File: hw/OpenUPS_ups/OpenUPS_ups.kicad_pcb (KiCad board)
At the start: 4 copper layers, 96 x 64 mm, 332 parts, among them J1001 USB4105-GF-A, J101 Barrel Jack, J102 XT30PW-M, J103 B6B-PH-K_1x06, J105 S6B-PH-K_1x06, J106 Screw Terminal, J107 Screw Terminal, J108 Screw Terminal, J109 JST XH, J110 JST XH, J501 Conn_01x03, J701 0022053031, J702 0022053031, J901 Qwiic, J902 Qwiic, Q1001 2N7002, Q1101 AON7534, Q1102 AON7534, Q1103 BSS84, Q1104 BSS84, Q1105 2N7002, Q1106 2N7002, Q1107 BSS84, Q301 AON7534, Q302 AON7534, Q303 AON7534, Q304 AON7534, Q401 2N7002, Q402 AON7534, Q403 AON7534, Q404 AON7534, Q405 AON7534, Q406 AON7423, Q601 AON7534, Q602 AON7534, Q603 AON7534, Q604 AON7534, Q701 2N7002, Q702 2N7002, U1001 MCP6547, U1002 AP22814BW5, U1003 NUP2301MW6T1G, U103 LM75BTP,147, U104 AVR64DB48x-x6LX, U1101 BQ76920PW, U1102 π220N31, U201 TPS51397A, U202 INA180A3, U301 NCP81599, U401 NCP431, U402 BD99950, U403 MCP6001R, U404 DZDH0401DW, U405 INA180A1, U601 NCP81599, U701 NUP2301MW6T1G, U702 NUP2301MW6T1G, U801 AP7383-33W5, U901 π220N31

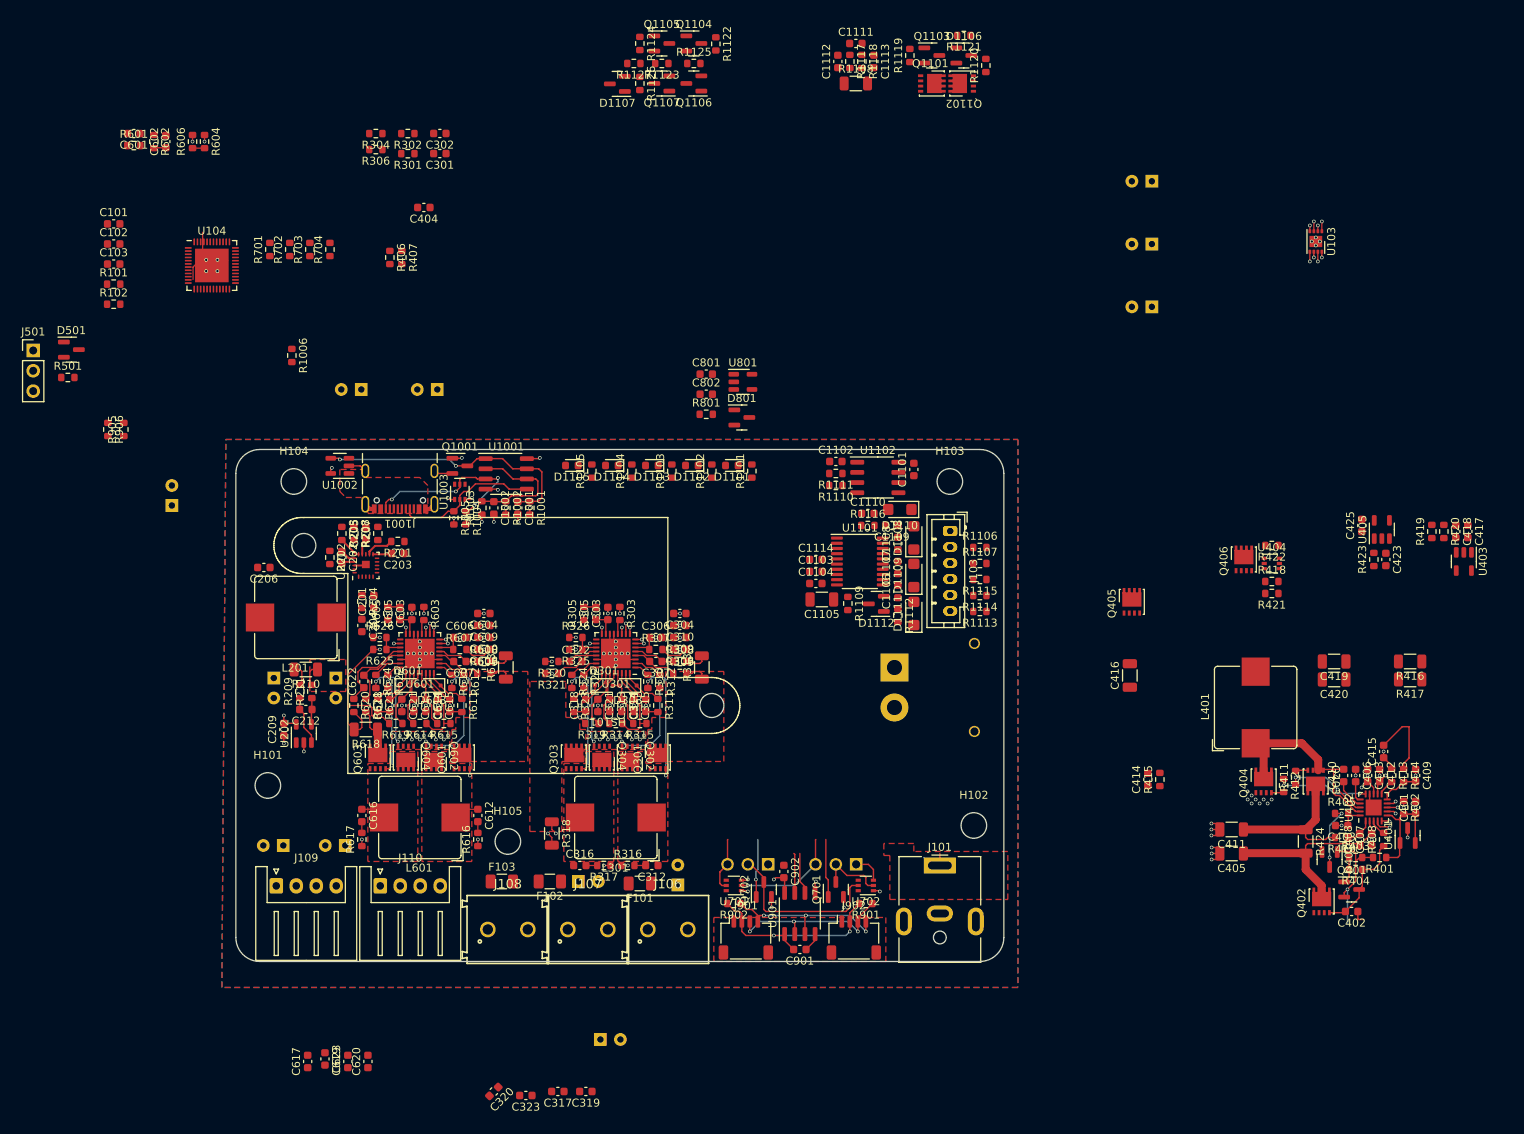
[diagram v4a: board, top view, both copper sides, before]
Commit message: BMS placement complete (no routing)
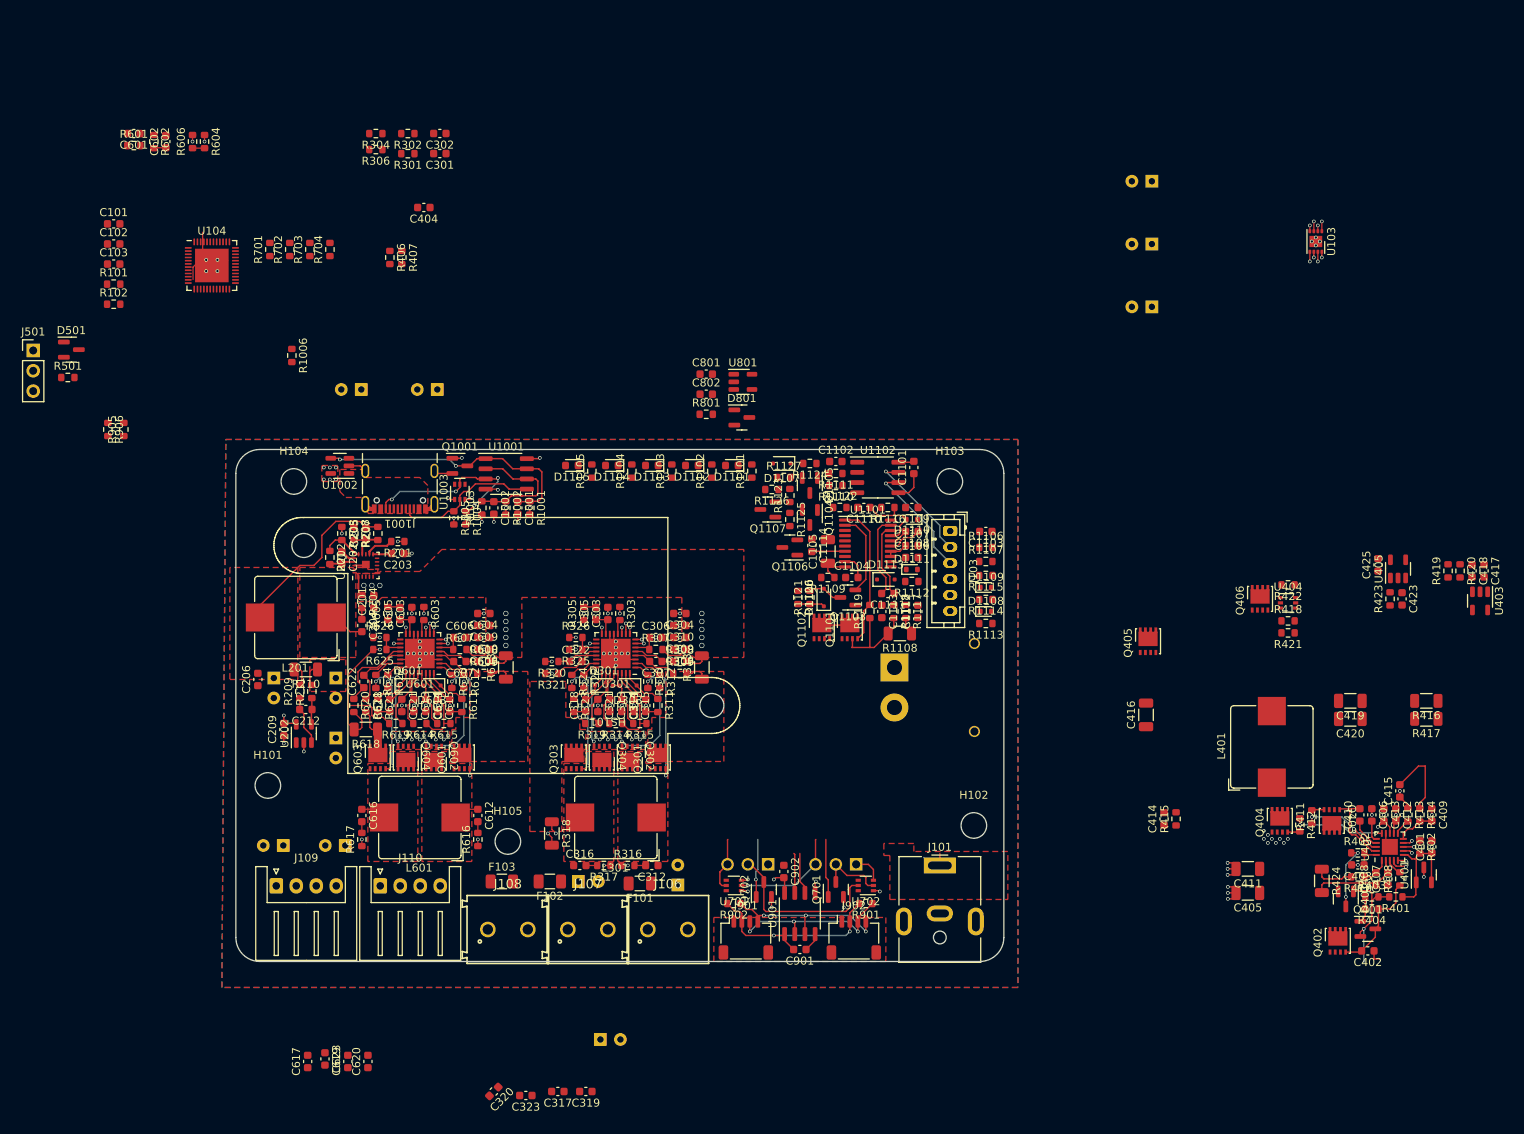
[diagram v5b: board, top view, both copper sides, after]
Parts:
- removed D1112: BAT54, Package_TO_SOT_SMD:SOT-23
- added D1113: BAT54J, Diode_SMD:D_SOD-323F, F.Cu at (164.2, 86.2)
- D1106, D1107: value BAT54 -> BAT54J; footprint Package_TO_SOT_SMD:SOT-23 -> Diode_SMD:D_SOD-323F
- D1108, D1109, D1110, D1111: value SMF5V0A -> ESD5Z5V0-DIO; footprint Diode_SMD:D_SMF -> Diode_SMD:D_SOD-523
- moved R1121 72.8 mm to (154.8, 88.5), turned to 90 degrees
- moved R1120 70.5 mm to (153.2, 88.5), turned to -90 degrees
- moved Q1102 70.2 mm to (156.2, 92.2), turned to 90 degrees
- moved D1106 70.0 mm to (156.5, 88.5), turned to 90 degrees
- moved R1119 69.7 mm to (162.2, 90.2)
- moved C1112 69.5 mm to (168.2, 90.2)
- moved R1117 69.1 mm to (166.8, 90.2)
- moved R1108 69.0 mm to (166.0, 93.0), turned to 180 degrees
- moved C1111 68.9 mm to (164.5, 88.0), turned to 180 degrees
- moved R1118 68.9 mm to (165.2, 90.2)
- moved Q1101 68.8 mm to (159.8, 92.2), turned to 90 degrees
- moved C1113 68.8 mm to (163.8, 90.2)
- moved Q1103 68.6 mm to (159.5, 88.5), turned to 180 degrees
- moved Q1104 61.0 mm to (154.8, 78.5), turned to -90 degrees
- moved R1122 60.0 mm to (158.5, 77.2), turned to 0 degrees
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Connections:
- C1106 pad 2: Net-(D1109-A1) -> Net-(D1108-A1)
- C1107 pad 1: Net-(D1109-A1) -> Net-(D1108-A1)
- C1107 pad 2: Net-(D1108-A1) -> Net-(D1108-A2)
- C1108 pad 1: Net-(D1108-A1) -> Net-(D1108-A2)
- C1108 pad 2: Net-(D1108-A2) -> Net-(D1109-A2)
- C1109 pad 1: Net-(D1108-A2) -> Net-(D1109-A2)
- D1106 pad 1: Net-(D1106-A) -> Net-(D1106-K)
- D1106 pad 2: unconnected-(D1106-NC-Pad2) -> Net-(D1106-A)
- D1107 pad 1: /BMS_ALERT -> +3.3VA
- D1107 pad 2: unconnected-(D1107-NC-Pad2) -> /BMS_ALERT
- D1109 pad 1: Net-(D1109-A1) -> Net-(D1108-A2)
- D1109 pad 2: Net-(D1108-A1) -> Net-(D1109-A2)
- D1110 pad 1: Net-(D1108-A2) -> Net-(D1109-A2)
- D1111 pad 2: Net-(D1109-A1) -> Net-(D1108-A1)
- J102 pad 1: +BATT -> -BATT
- J102 pad 2: -BATT -> +BATT
- R1113 pad 1: Net-(D1109-A1) -> Net-(D1108-A1)
- R1114 pad 1: Net-(D1108-A1) -> Net-(D1108-A2)
- R1115 pad 1: Net-(D1108-A2) -> Net-(D1109-A2)
- U1101 pad 13: Net-(D1109-A1) -> Net-(D1108-A1)
- U1101 pad 14: Net-(D1109-A1) -> Net-(D1108-A1)
- U1101 pad 15: Net-(D1108-A1) -> Net-(D1108-A2)
- U1101 pad 16: Net-(D1108-A2) -> Net-(D1109-A2)
- U201 pad 9: /5V Buck/PG -> GND
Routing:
- net Net-(C205-Pad2): track 2.84 -> 25.4 mm
- net Net-(Q1101-G): track 0.00 -> 17.7 mm
- net /BMS/BMS_SCL: track 0.00 -> 15.0 mm, vias 0 -> 1
- net Net-(U402-PHASE): track 24.7 -> 9.83 mm
- net /BMS/BMS_SDA: track 0.00 -> 14.4 mm, vias 0 -> 1
- net Net-(U402-ACP): track 26.3 -> 12.0 mm
- net /Aux Power Supplies/EN2: track 18.6 -> 4.59 mm
- net Net-(Q1101-S-Pad1): track 0.00 -> 12.3 mm
- net Net-(Q1103-S): track 0.00 -> 10.5 mm
- net Net-(U1101-SRN): track 0.00 -> 10.5 mm
- net Net-(D1110-A2): track 0.00 -> 9.51 mm
- net Net-(U1101-SRP): track 0.00 -> 9.34 mm
- net -BATT: track 0.00 -> 5.89 mm
- net Net-(C204-Pad2): track 0.00 -> 4.51 mm
- net GND: track 99.5 -> 103.9 mm, vias 121 -> 126
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- added copper zone on F.Cu, net Net-(C204-Pad2)
- added copper zone on F.Cu, net Net-(C205-Pad2)
- added copper zone on F.Cu, net Vsys

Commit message: Batt charger placement
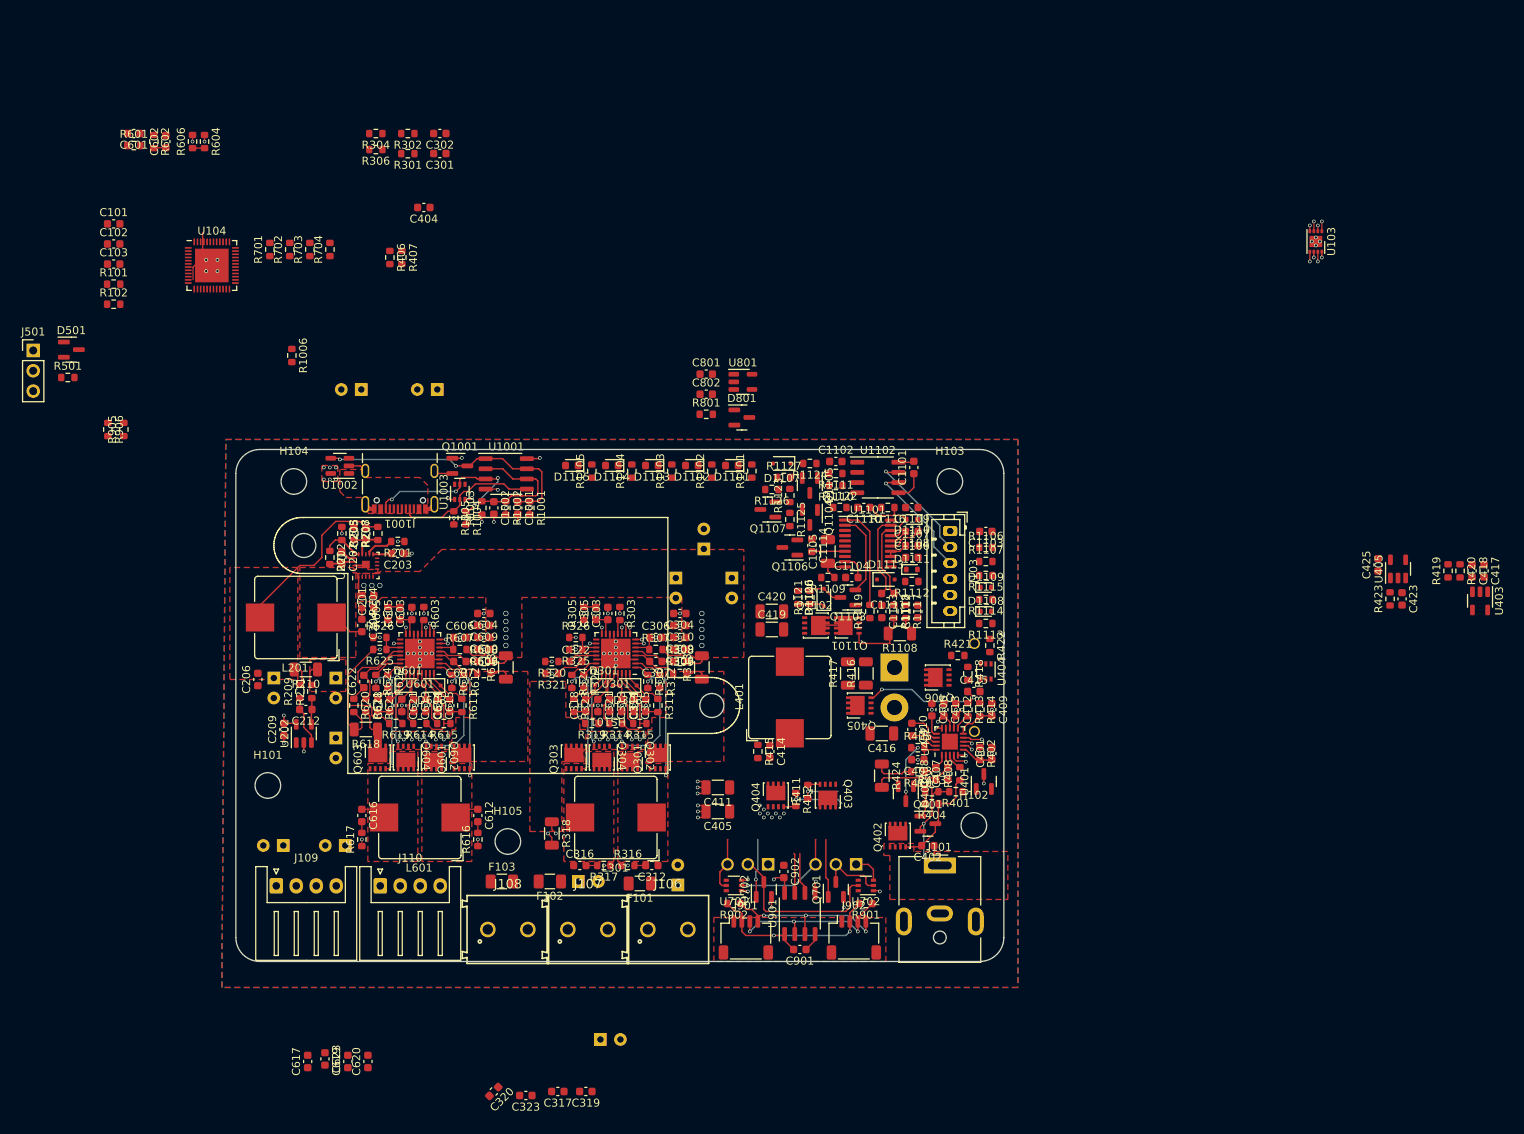
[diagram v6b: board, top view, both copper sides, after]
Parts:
- moved C424 77.5 mm to (138.0, 86.1), turned to -90 degrees
- moved C420 73.5 mm to (150.0, 90.2), turned to 0 degrees
- moved C419 72.9 mm to (150.0, 92.5), turned to 0 degrees
- moved R417 72.5 mm to (159.5, 98.0), turned to 90 degrees
- moved R416 70.1 mm to (161.8, 98.0), turned to 90 degrees
- moved C426 67.1 mm to (145.0, 86.1), turned to -90 degrees
- moved C405 67.0 mm to (143.2, 115.2)
- moved C411 67.0 mm to (143.2, 112.2)
- moved C427 63.7 mm to (141.5, 82.4), turned to 90 degrees
- moved Q403 63.1 mm to (157.0, 113.2)
- moved Q404 63.1 mm to (150.5, 113.2)
- moved R411 63.1 mm to (154.5, 112.8)
- moved R412 63.1 mm to (153.0, 113.8)
- moved L401 60.6 mm to (152.2, 101.0)
- moved C410 57.0 mm to (167.5, 105.0), turned to -90 degrees
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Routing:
- net Net-(Q405-G): track 2.59 -> 16.2 mm, vias 1 -> 2
- net Net-(U401-K): track 14.1 -> 4.05 mm
- net +BATT: track 13.0 -> 3.32 mm
- net Net-(U402-PHASE): track 9.83 -> 3.58 mm
- net Net-(Q1101-G): track 17.7 -> 12.9 mm
- net Net-(U402-LDRV): track 11.5 -> 7.56 mm
- net Net-(Q1101-S-Pad1): track 12.3 -> 8.62 mm
- net Net-(U402-HDRV): track 10.4 -> 7.11 mm
- net /I2C_I_SCL: track 4.48 -> 5.72 mm

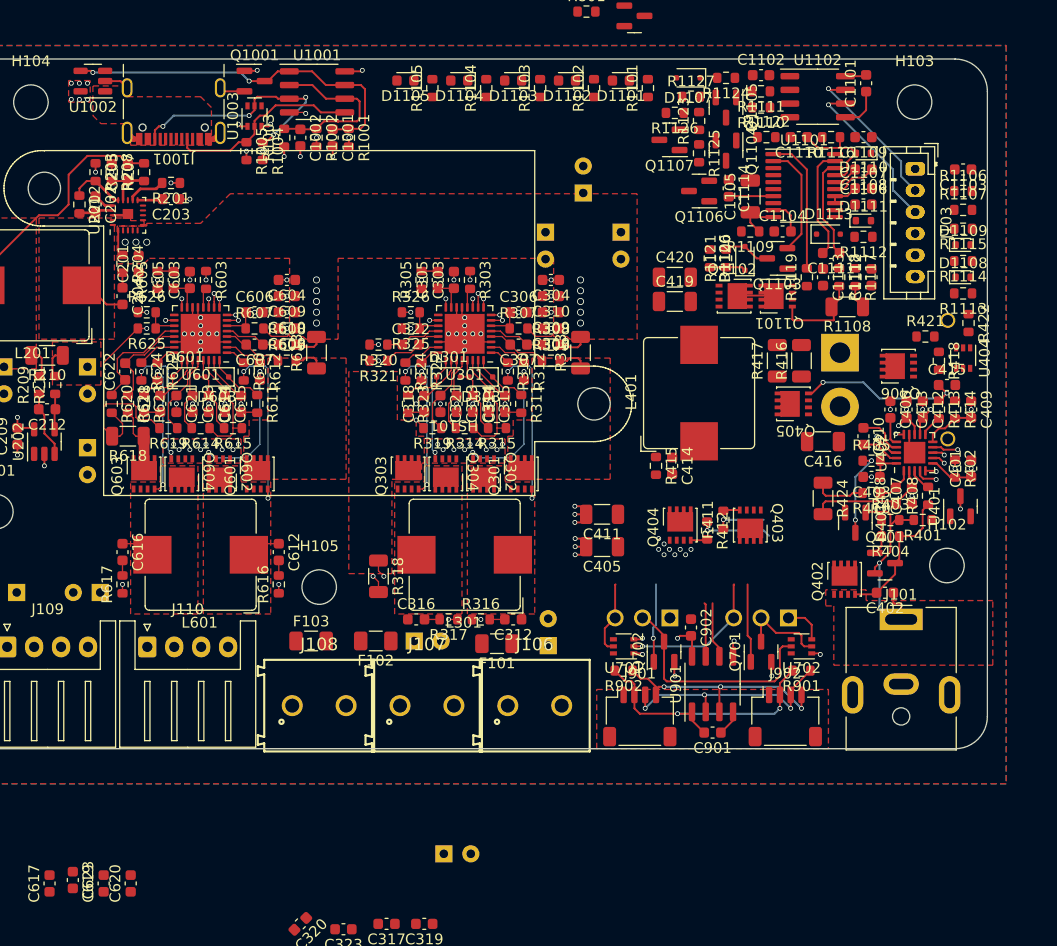
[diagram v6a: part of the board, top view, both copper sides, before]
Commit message: East Side layout and routing
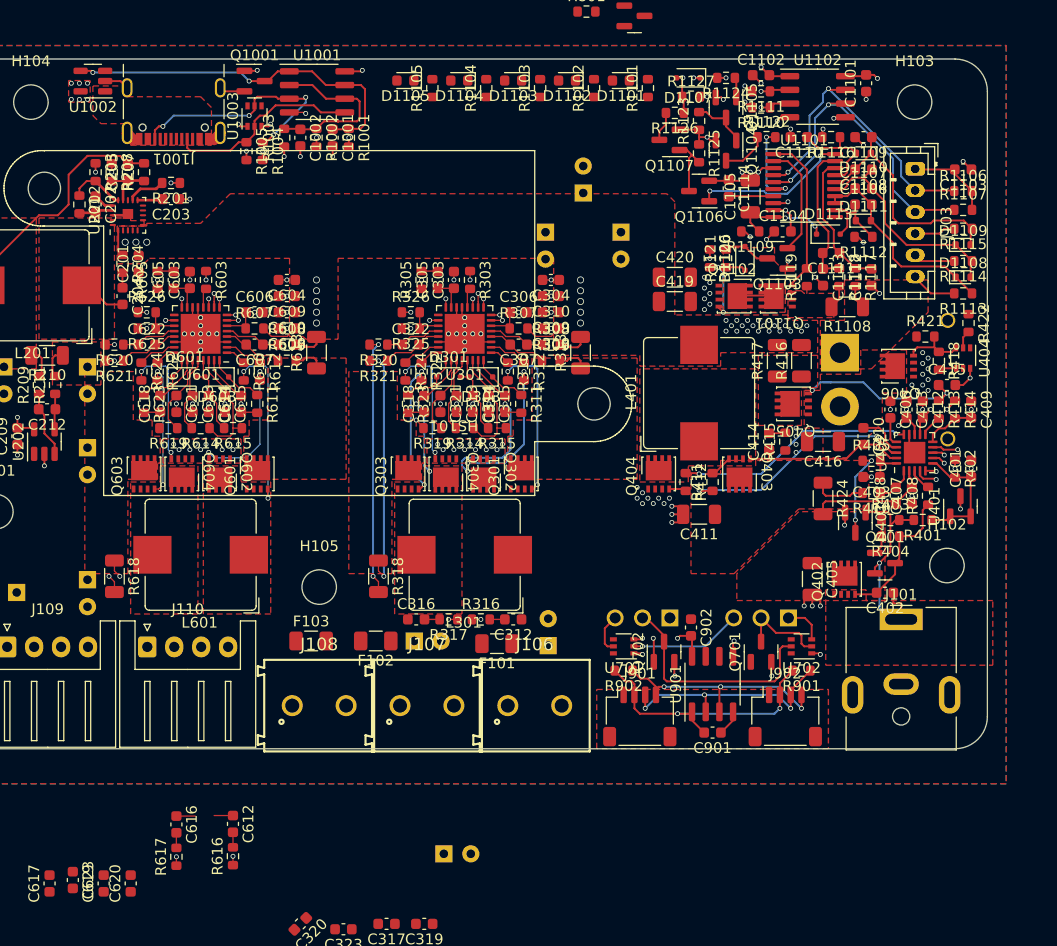
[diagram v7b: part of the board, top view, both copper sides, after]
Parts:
- moved C616 25.8 mm to (103.8, 141.0)
- moved R617 25.8 mm to (103.8, 144.0)
- moved C612 25.6 mm to (109.0, 141.0)
- moved R616 25.6 mm to (109.0, 144.0)
- moved C405 19.7 mm to (162.8, 118.2), turned to -90 degrees
- moved R618 13.1 mm to (98.0, 118.0), turned to -90 degrees
- moved R415 12.2 mm to (160.2, 105.5), turned to 90 degrees
- moved C414 9.28 mm to (158.8, 105.5), turned to 90 degrees
- moved C411 9.00 mm to (152.2, 112.2)
- moved R620 5.51 mm to (98.0, 96.5), turned to 180 degrees
- moved Q404 5.15 mm to (148.5, 108.5)
- moved R412 4.92 mm to (151.0, 109.2)
- moved Q403 4.85 mm to (156.0, 108.5)
- moved R621 4.19 mm to (98.0, 98.0), turned to 180 degrees
- moved R411 3.64 mm to (153.5, 109.2)
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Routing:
- net +BATT: track 3.32 -> 69.6 mm, vias 0 -> 6
- net Vsys: track 15.7 -> 57.4 mm, vias 14 -> 47
- net VBMS: track 1.98 -> 34.0 mm, vias 0 -> 2
- net +AdjV: track 4.35 -> 26.1 mm
- net Net-(Q303-D-Pad5): track 2.49 -> 22.7 mm
- net Net-(D1109-A2): track 2.35 -> 22.4 mm
- net +12V: track 26.5 -> 7.09 mm, vias 1 -> 3
- net Net-(D1108-A1): track 2.81 -> 19.5 mm
- net Net-(D1108-A2): track 4.30 -> 20.4 mm
- net Net-(U402-HDRV): track 7.11 -> 22.4 mm
- net Net-(U402-LDRV): track 7.56 -> 22.1 mm
- net Net-(Q1106-G): track 0.00 -> 14.5 mm, vias 0 -> 2
- net /BMS/BMS_SCL: track 15.0 -> 29.4 mm, vias 1 -> 2
- net /BMS/BMS_SDA: track 14.4 -> 28.8 mm, vias 1 -> 2
- net -BATT: track 5.89 -> 19.8 mm, vias 0 -> 13
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- added copper zone on F.Cu, net +BATT
- added copper zone on F.Cu, net -BATT
- added copper zone on In1.Cu, net -BATT
- added copper zone on F.Cu, net /Aux Power Supplies/EN2
- added copper zone on F.Cu, net /Bat_Charger/B_SRN
- added copper zone on F.Cu, net Net-(Q1101-D-Pad5)
- added copper zone on F.Cu, net Net-(Q1101-S-Pad1)
- added copper zone on F.Cu, net Net-(Q603-D-Pad5)
- added copper zone on F.Cu, net Net-(U402-ACP)
- added copper zone on F.Cu, net Net-(U402-PHASE)
- removed copper zone on F.Cu, net Net-(U301B-VSW1)
